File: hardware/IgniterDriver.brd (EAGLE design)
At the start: 47 x 40.5 mm, 48 parts, among them IC1 4066D, Q2 TJ8S06M3L(T6L1,NQ), U1 ACS711ELCTR-12AB-T

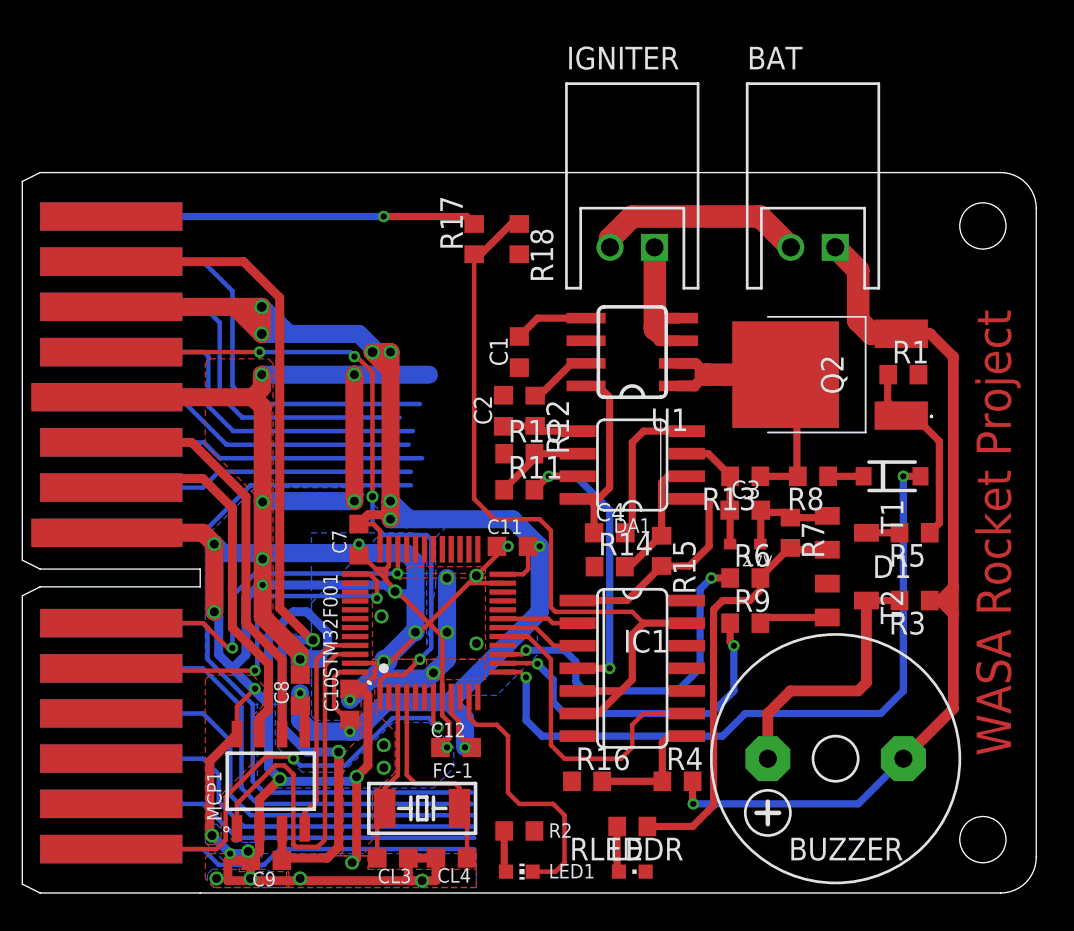
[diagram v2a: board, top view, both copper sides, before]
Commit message: Complete igniter driver board
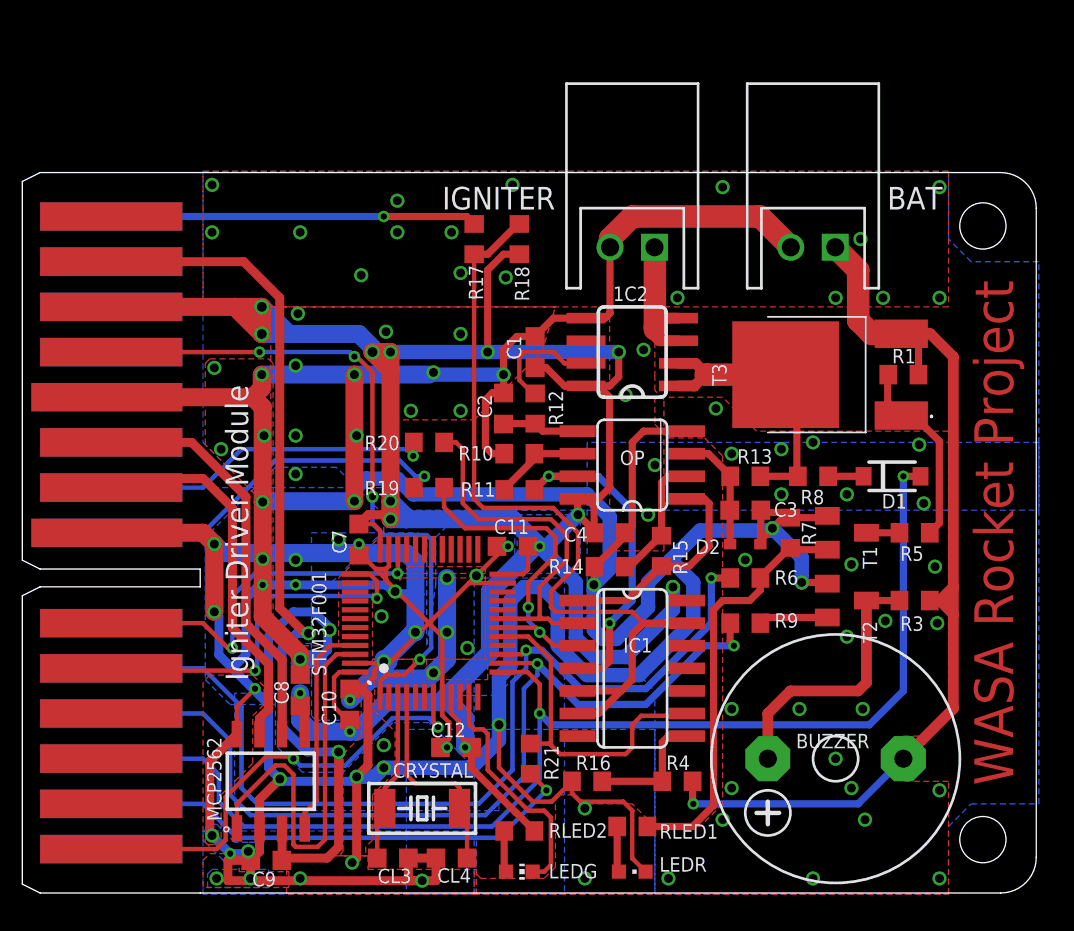
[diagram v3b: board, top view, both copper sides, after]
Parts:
- added R19, R20, R21: 1k, resistor:R0603
- moved C1 0.89 mm to (28.8, 10.2)
- moved C2 0.13 mm to (27.1, 6.99)
- moved R12 0.13 mm to (28.8, 6.99)
- renumbered 2.7V to D2, DA1 to OP, FC-1 to CRYSTAL, LED1 to LEDG, MCP1 to MCP2562, Q2 to T3, R2 to RLED2, RLED to RLED1, U1 to 1C2
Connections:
- net VBAT renamed VBU
- removed net N$46: U$2.30
- removed net N$48: U$2.28
- removed net N$49: U$2.27
- removed net N$50: U$2.26
- removed net N$51: U$2.25
- removed net N$54: U$2.21
- removed net N$55: U$2.20
- removed net N$56: U$2.19
- removed net N$57: U$2.18
- removed net N$82: U$2.17
- net BUZZER: now also U$2.27
- net CIG: now also R19.1
- net IGNITE: now also U$2.26
- net N$47: now also R21.2
- net N$52: now also R19.2
- net N$53: now also R20.2
- net TEST: now also U$2.28
- net VBAT+: now also R21.1
- net VIG: now also R20.1
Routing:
- net GND: track 244.9 -> 363.4 mm, vias 35 -> 106
- net VDD: track 101.8 -> 155.5 mm, vias 10 -> 14
- net IGNITE: track 19.7 -> 54.1 mm
- net BUZZER: track 19.3 -> 51.6 mm
- net TEST: track 39.5 -> 69.9 mm
- net N$51: track 27.8 -> 0.00 mm
- net N$50: track 26.1 -> 0.00 mm
- net N$49: track 24.6 -> 0.00 mm
- net N$82: track 23.8 -> 0.00 mm
- net N$48: track 22.9 -> 0.00 mm
- net N$57: track 21.2 -> 0.00 mm
- net N$46: track 21.1 -> 0.00 mm
- net N$56: track 20.4 -> 0.00 mm
- net N$54: track 18.0 -> 0.00 mm
- net N$55: track 17.8 -> 0.00 mm
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- added copper zone on layer 16, net VDD
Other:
- board text added: "Designed by @fujiy0, 2019"
- board text added: "Igniter Driver Module"

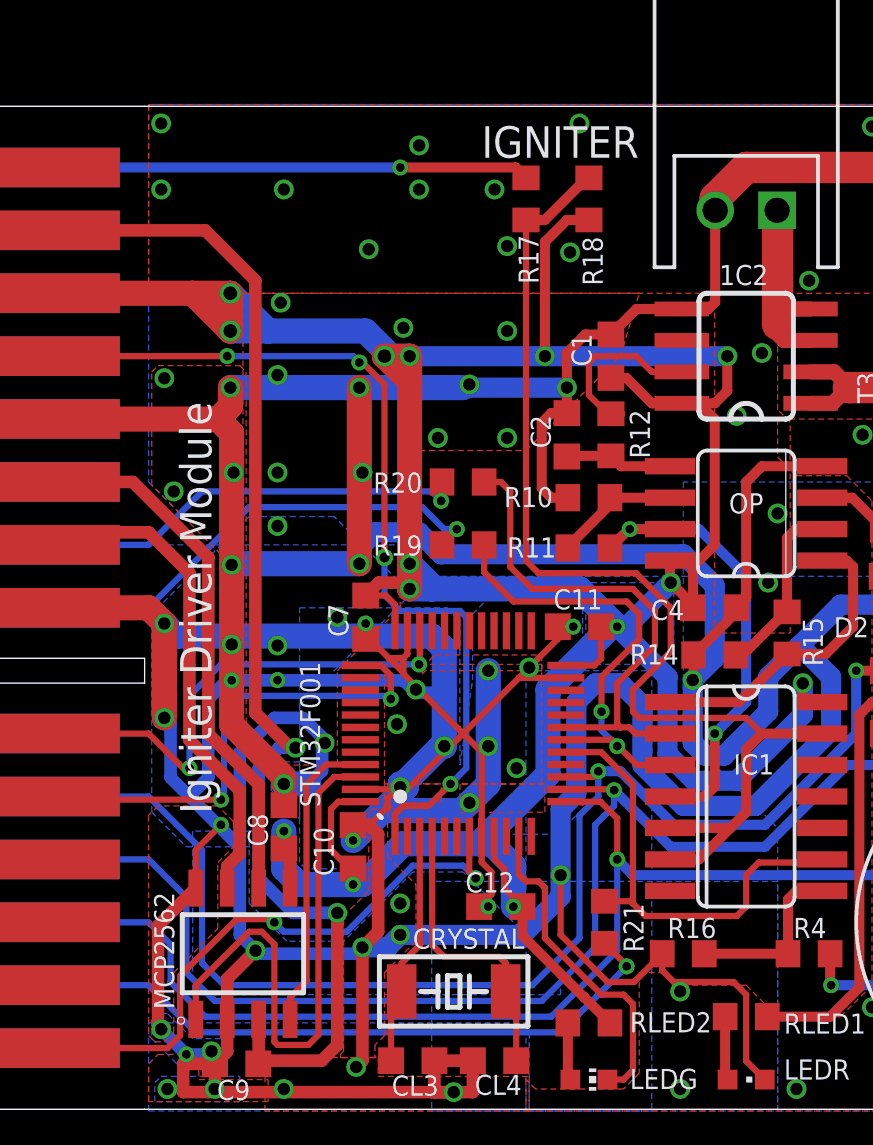
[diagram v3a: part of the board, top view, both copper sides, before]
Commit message: Clean silk print
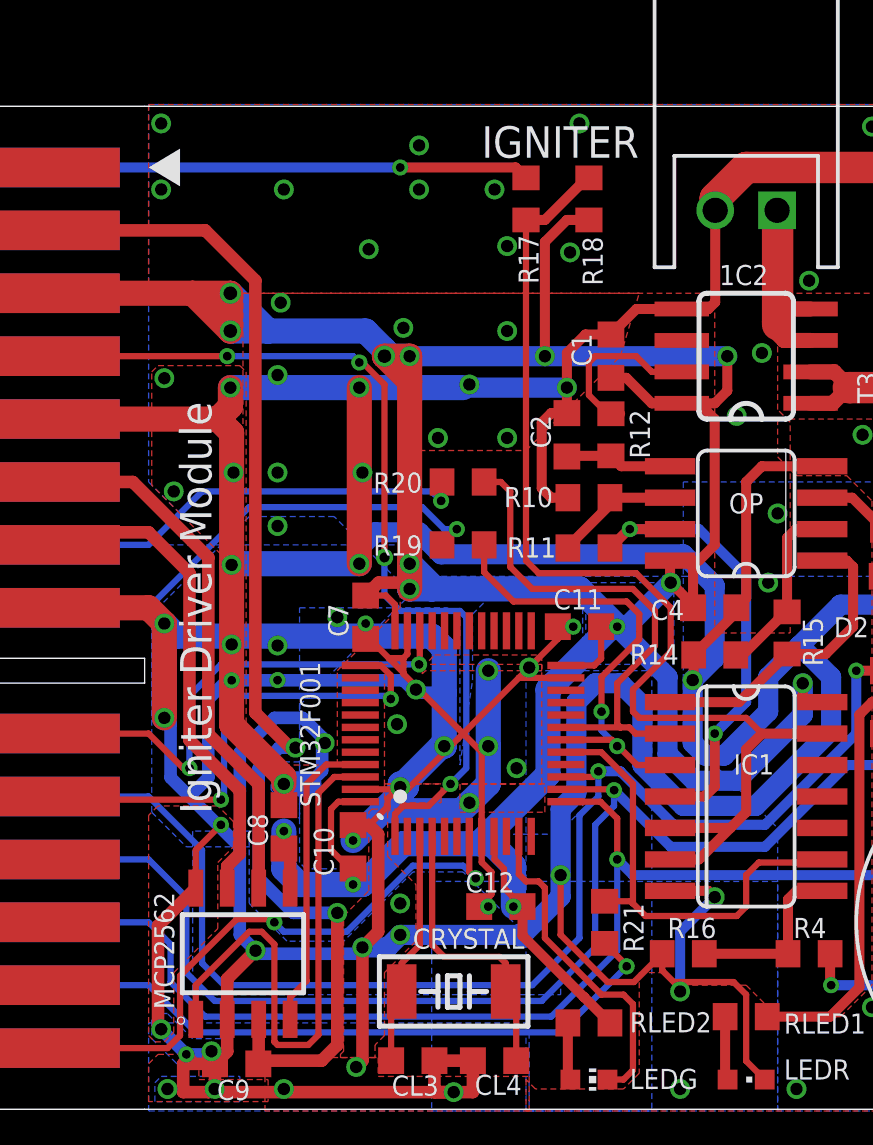
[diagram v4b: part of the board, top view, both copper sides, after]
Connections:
- removed net VSS: IC1.7
- net GND: now also IC1.7
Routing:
- net GND: track 363.4 -> 369.7 mm, vias 106 -> 107
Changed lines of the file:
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@@
 <layer number="14" name="Route14" color="22" fill="1" visible="no" active="no"/>
 <layer number="15" name="Route15" color="23" fill="1" visible="no" active="no"/>
-<layer number="16" name="Bottom" color="1" fill="1" visible="no" active="yes"/>
+<layer number="16" name="Bottom" color="1" fill="1" visible="yes" active="yes"/>
 <layer number="17" name="Pads" color="2" fill="1" visible="yes" active="yes"/>
 <layer number="18" name="Vias" color="2" fill="1" visible="yes" active="yes"/>
@@
 <layer number="20" name="Dimension" color="24" fill="1" visible="yes" active="yes"/>
 <layer number="21" name="tPlace" color="7" fill="1" visible="yes" active="yes"/>
-<layer number="22" name="bPlace" color="7" fill="1" visible="no" active="yes"/>
+<layer number="22" name="bPlace" color="7" fill="1" visible="yes" active="yes"/>
 <layer number="23" name="tOrigins" color="15" fill="1" visible="yes" active="yes"/>
-<layer number="24" name="bOrigins" color="15" fill="1" visible="no" active="yes"/>
+<layer number="24" name="bOrigins" color="15" fill="1" visible="yes" active="yes"/>
 <layer number="25" name="tNames" color="7" fill="1" visible="yes" active="yes"/>
-<layer number="26" name="bNames" color="7" fill="1" visible="no" active="yes"/>
+<layer number="26" name="bNames" color="7" fill="1" visible="yes" active="yes"/>
 <layer number="27" name="tValues" color="7" fill="1" visible="no" active="yes"/>
 <layer number="28" name="bValues" color="7" fill="1" visible="no" active="yes"/>
-<layer number="29" name="tStop" color="7" fill="3" visible="yes" active="yes"/>
+<layer number="29" name="tStop" color="7" fill="3" visible="no" active="yes"/>
 <layer number="30" name="bStop" color="7" fill="6" visible="no" active="yes"/>
 <layer number="31" name="tCream" color="7" fill="4" visible="no" active="yes"/>
@@
 <layer number="38" name="bTest" color="7" fill="1" visible="no" active="yes"/>
 <layer number="39" name="tKeepout" color="4" fill="11" visible="yes" active="yes"/>
-<layer number="40" name="bKeepout" color="1" fill="11" visible="no" active="yes"/>
+<layer number="40" name="bKeepout" color="1" fill="11" visible="yes" active="yes"/>
 <layer number="41" name="tRestrict" color="4" fill="10" visible="yes" active="yes"/>
-<layer number="42" name="bRestrict" color="1" fill="10" visible="no" active="yes"/>
+<layer number="42" name="bRestrict" color="1" fill="10" visible="yes" active="yes"/>
 <layer number="43" name="vRestrict" color="2" fill="10" visible="no" active="yes"/>
 <layer number="44" name="Drills" color="7" fill="1" visible="no" active="yes"/>
@@
 <layer number="50" name="dxf" color="7" fill="1" visible="no" active="no"/>
 <layer number="51" name="tDocu" color="7" fill="1" visible="yes" active="yes"/>
-<layer number="52" name="bDocu" color="7" fill="1" visible="no" active="yes"/>
+<layer number="52" name="bDocu" color="7" fill="1" visible="yes" active="yes"/>
 <layer number="53" name="tGND_GNDA" color="7" fill="9" visible="no" active="no"/>
 <layer number="54" name="bGND_GNDA" color="1" fill="9" visible="no" active="no"/>
@@
 <text x="55.88" y="-7.62" size="0.8128" layer="30" font="vector" rot="MR270" align="center">Designed by @fujiy0, 2019</text>
 <text x="12.065" y="0" size="1.27" layer="25" font="vector" rot="R90" align="center">Igniter Driver Module</text>
+<polygon width="0" layer="21">
+<vertex x="10.16" y="17.78"/>
+<vertex x="11.43" y="18.542"/>
+<vertex x="11.43" y="17.018"/>
+</polygon>
 </plain>
 <attributes>
@@
 <vertex x="29.21" y="10.16"/>
 <vertex x="29.972" y="12.7"/>
-<vertex x="29.972" y="12.7"/>
 </polygon>
 <polygon width="0" layer="1" rank="2">
@@
 <via x="17.78" y="-0.381" extent="1-16" drill="0.5"/>
 <via x="15.367" y="-2.921" extent="1-16" drill="0.35"/>
+<contactref element="IC1" pad="7"/>
+<wire x1="31.2166" y1="-11.43" x2="32.766" y2="-11.43" width="0.4064" layer="1"/>
+<wire x1="32.766" y1="-11.43" x2="33.02" y2="-11.684" width="0.4064" layer="1"/>
+<via x="33.02" y="-11.684" extent="1-16" drill="0.5"/>
+<wire x1="33.02" y1="-11.684" x2="31.623" y2="-13.081" width="0.4064" layer="16"/>
+<wire x1="31.623" y1="-13.081" x2="31.623" y2="-15.494" width="0.4064" layer="16"/>
 </signal>
 <signal name="VDD">
@@
 <wire x1="28.956" y1="-8.001" x2="28.194" y2="-8.763" width="0.254" layer="16"/>
 </signal>
-<signal name="VSS">
-<contactref element="IC1" pad="7"/>
-</signal>
 <signal name="VIG'">
